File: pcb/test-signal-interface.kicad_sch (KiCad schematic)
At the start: 7 parts, among them J2 BSE-040-01-F-D-A-TR, J3 BSE-040-01-F-D-A-TR, U1 AT24C64D-SSHM-T

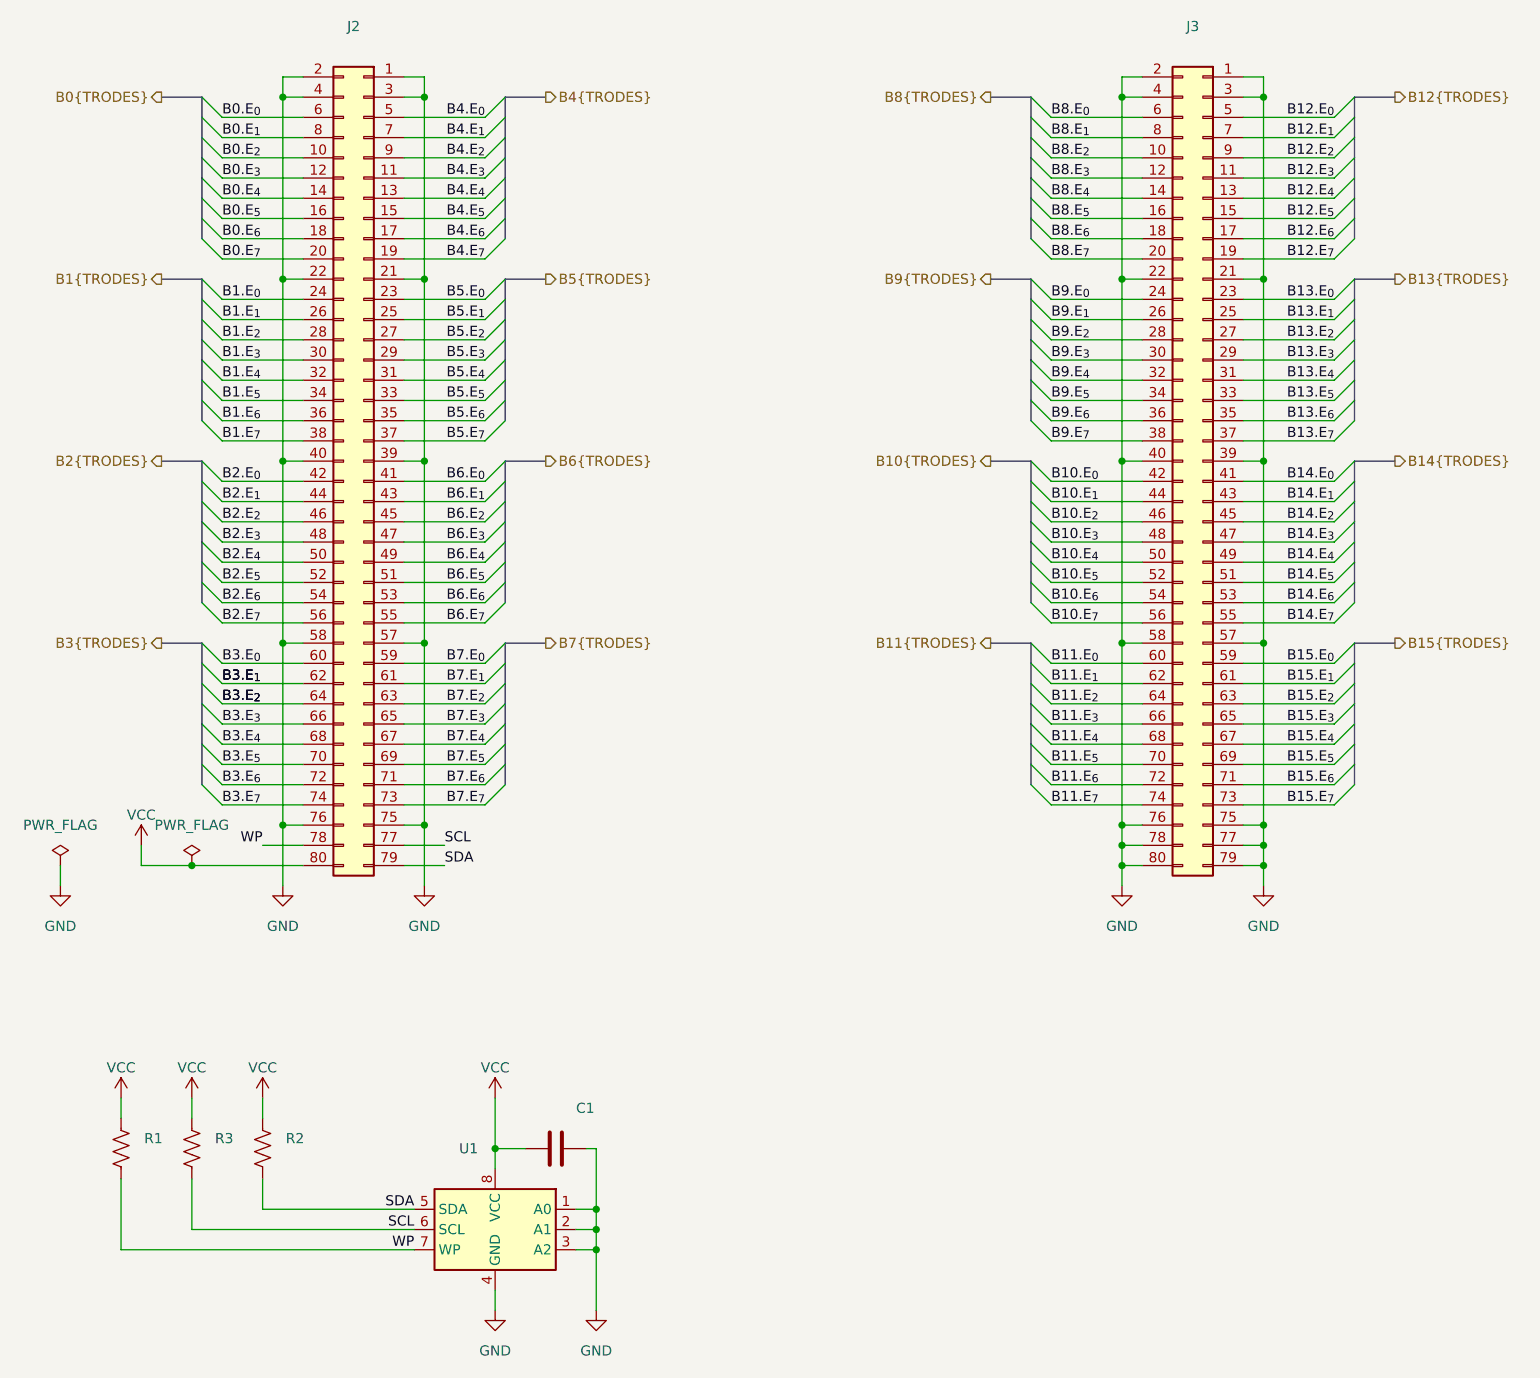
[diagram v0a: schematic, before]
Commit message: details & manufacturing files
- chaged via size D=0.5mm & H=0.2mm
- generated production files
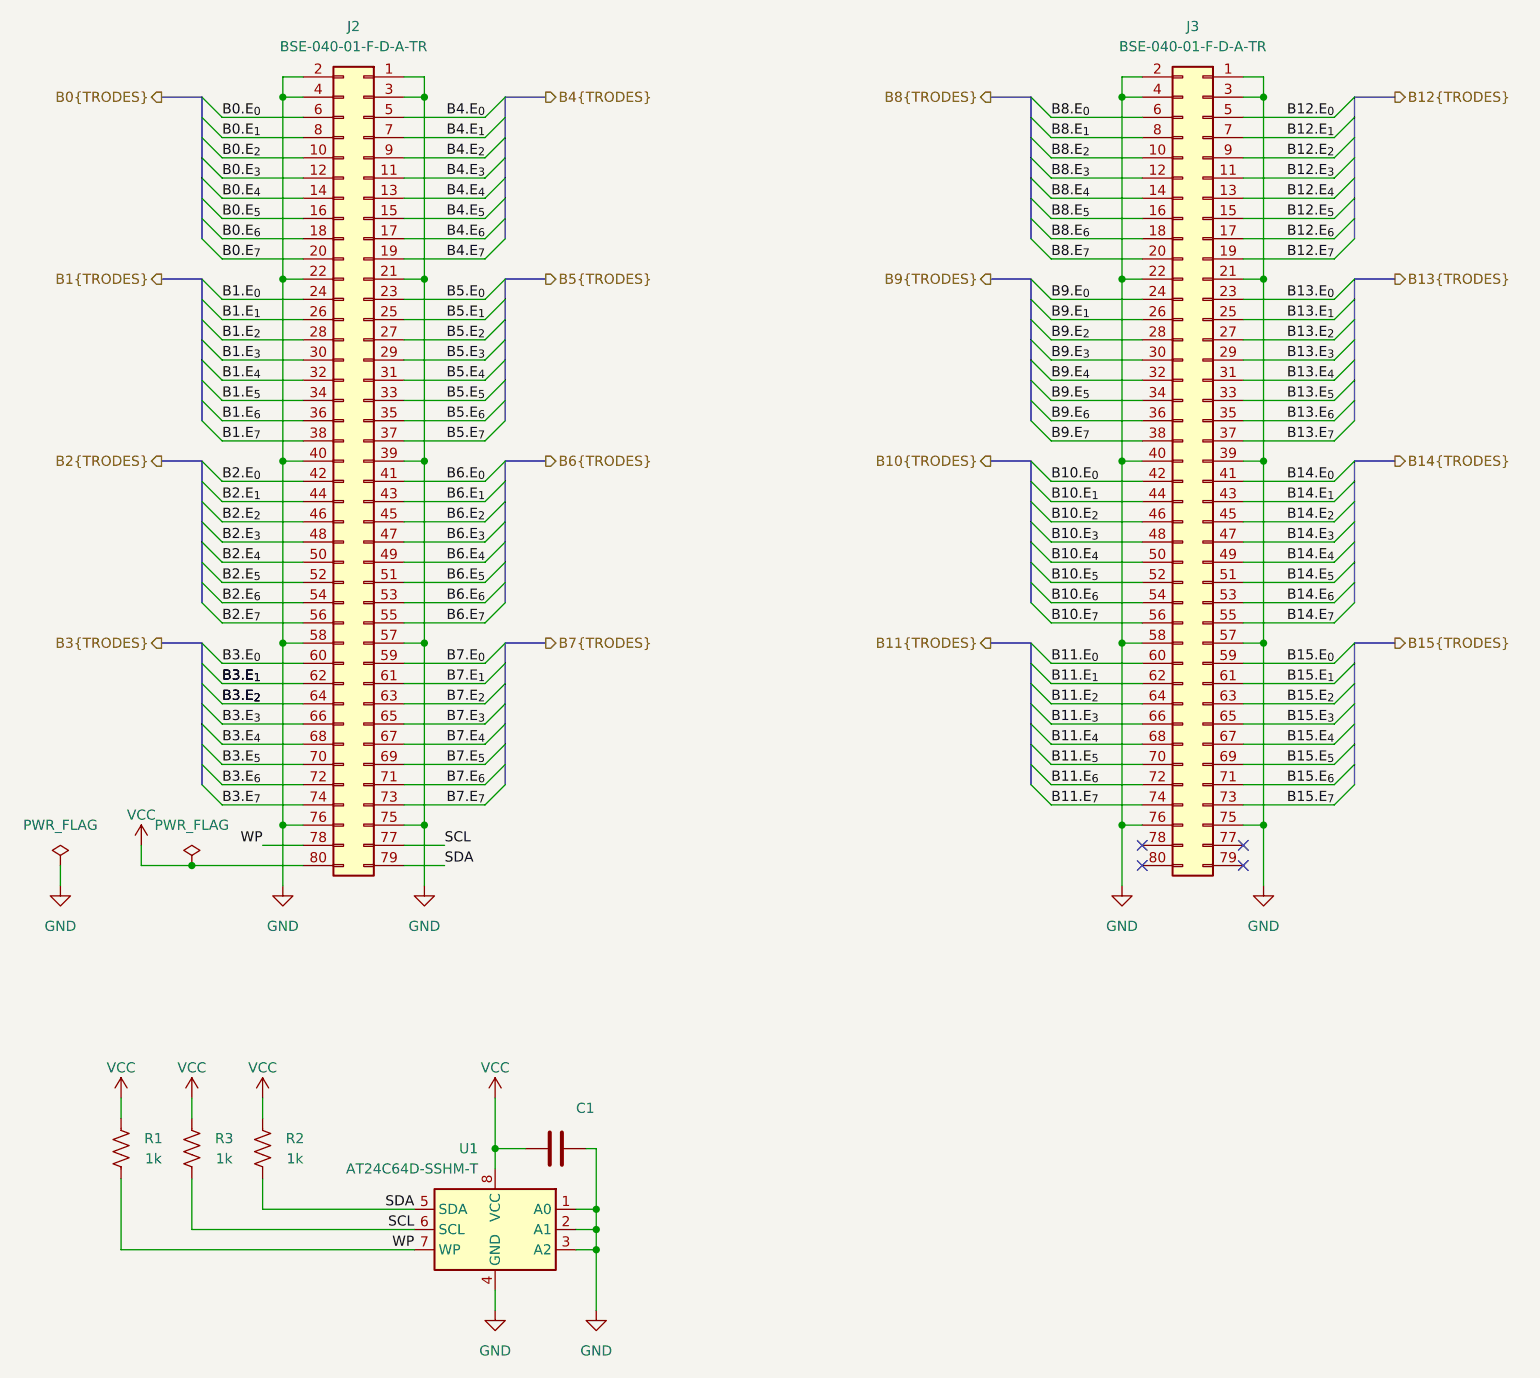
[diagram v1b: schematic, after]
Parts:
- J2, J3: MPN BSE-040-01-X-D-A -> BSE-040-01-F-D-A-TR
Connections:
- net GND: no longer J3.77 (Pin_77), J3.78 (Pin_78), J3.79 (Pin_79), J3.80 (Pin_80)
- no-connect marks 0 -> 4
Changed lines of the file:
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@@
 	)
 	(junction
-		(at 186.69 124.46)
-		(diameter 0)
-		(color 0 0 0 0)
-	)
-	(junction
-		(at 204.47 127)
-		(diameter 0)
-		(color 0 0 0 0)
-	)
-	(junction
 		(at 99.06 53.34)
 		(diameter 0)
@@
 	)
 	(junction
-		(at 186.69 127)
-		(diameter 0)
-		(color 0 0 0 0)
-	)
-	(junction
 		(at 204.47 76.2)
 		(diameter 0)
@@
 	)
 	(junction
-		(at 204.47 124.46)
-		(diameter 0)
-		(color 0 0 0 0)
-	)
-	(junction
 		(at 204.47 53.34)
 		(diameter 0)
@@
 		(color 0 0 0 0)
 	)
+	(no_connect
+		(at 189.23 127)
+	)
+	(no_connect
+		(at 189.23 124.46)
+	)
+	(no_connect
+		(at 201.93 127)
+	)
+	(no_connect
+		(at 201.93 124.46)
+	)
 	(bus_entry
 		(at 71.12 101.6)
@@
 	(wire
 		(pts
-			(xy 186.69 121.92) (xy 186.69 124.46)
+			(xy 186.69 121.92) (xy 186.69 129.54)
 		)
 		(stroke
@@
 	(wire
 		(pts
-			(xy 189.23 124.46) (xy 186.69 124.46)
-		)
-		(stroke
-			(width 0)
-			(type default)
-		)
-	)
-	(wire
-		(pts
 			(xy 73.66 63.5) (xy 83.82 63.5)
 		)
@@
 		)
 	)
-	(wire
-		(pts
-			(xy 204.47 121.92) (xy 204.47 124.46)
-		)
-		(stroke
-			(width 0)
-			(type default)
-		)
-	)
 	(bus
 		(pts
@@
 		)
 	)
-	(wire
-		(pts
-			(xy 186.69 129.54) (xy 186.69 127)
-		)
-		(stroke
-			(width 0)
-			(type default)
-		)
-	)
 	(bus
 		(pts
@@
 	(wire
 		(pts
-			(xy 204.47 127) (xy 204.47 129.54)
+			(xy 204.47 121.92) (xy 204.47 129.54)
 		)
 		(stroke
@@
 		)
 	)
-	(wire
-		(pts
-			(xy 201.93 124.46) (xy 204.47 124.46)
-		)
-		(stroke
-			(width 0)
-			(type default)
-		)
-	)
 	(bus
 		(pts
@@
 	(wire
 		(pts
-			(xy 204.47 124.46) (xy 204.47 127)
-		)
-		(stroke
-			(width 0)
-			(type default)
-		)
-	)
-	(wire
-		(pts
 			(xy 96.52 33.02) (xy 106.68 33.02)
 		)
@@
 	(wire
 		(pts
-			(xy 201.93 127) (xy 204.47 127)
-		)
-		(stroke
-			(width 0)
-			(type default)
-		)
-	)
-	(wire
-		(pts
 			(xy 201.93 83.82) (xy 213.36 83.82)
 		)
@@
 	(wire
 		(pts
-			(xy 186.69 127) (xy 189.23 127)
-		)
-		(stroke
-			(width 0)
-			(type default)
-		)
-	)
-	(wire
-		(pts
 			(xy 186.69 99.06) (xy 186.69 121.92)
 		)
@@
 	(wire
 		(pts
-			(xy 186.69 124.46) (xy 186.69 127)
-		)
-		(stroke
-			(width 0)
-			(type default)
-		)
-	)
-	(wire
-		(pts
 			(xy 177.8 116.84) (xy 189.23 116.84)
 		)
@@
 					(size 1.27 1.27)
 				)
-				(hide yes)
 			)
 		)
@@
 			)
 		)
-		(property "MPN" "BSE-040-01-X-D-A"
+		(property "MPN" "BSE-040-01-F-D-A-TR"
 			(at 91.44 76.2 0)
 			(effects
@@
 					(size 1.27 1.27)
 				)
-				(hide yes)
 			)
 		)
@@
 			)
 		)
-		(property "MPN" "BSE-040-01-X-D-A"
+		(property "MPN" "BSE-040-01-F-D-A-TR"
 			(at 196.85 76.2 0)
 			(effects
@@
 					(size 1.27 1.27)
 				)
-				(hide yes)
 			)
 		)
@@
 					(size 1.27 1.27)
 				)
-				(hide yes)
 			)
 		)
@@
 					(size 1.27 1.27)
 				)
-				(hide yes)
 			)
 		)
@@
 				)
 				(justify left)
-				(hide yes)
 			)
 		)

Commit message: Libraries links updated
Removed local Libraries from Project
. KiCAD libraries
. open-ephys kicad library
. jonnew library

Created new manufacturing files
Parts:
- J2, J3: footprint _footprint Lib:SAMTEC_BSE-040-01-X-D-A -> jonnew:SAMTEC_BSE-040-01-X-D-A; symbol _symbol Lib:Conn_02x40_Odd_Even -> Connector_Generic:Conn_02x40_Odd_Even
- U1: symbol _symbol Lib:AT24CS01-SSHM -> Memory_EEPROM:AT24CS01-SSHM
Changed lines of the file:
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@@
 	)
 	(symbol
-		(lib_id "_symbol Lib:Conn_02x40_Odd_Even")
+		(lib_id "Connector_Generic:Conn_02x40_Odd_Even")
 		(at 91.44 76.2 0)
 		(mirror y)
@@
 			)
 		)
-		(property "Footprint" "_footprint Lib:SAMTEC_BSE-040-01-X-D-A"
+		(property "Footprint" "jonnew:SAMTEC_BSE-040-01-X-D-A"
 			(at 91.44 76.2 0)
 			(effects
@@
 	)
 	(symbol
-		(lib_id "_symbol Lib:Conn_02x40_Odd_Even")
+		(lib_id "Connector_Generic:Conn_02x40_Odd_Even")
 		(at 196.85 76.2 0)
 		(mirror y)
@@
 			)
 		)
-		(property "Footprint" "_footprint Lib:SAMTEC_BSE-040-01-X-D-A"
+		(property "Footprint" "jonnew:SAMTEC_BSE-040-01-X-D-A"
 			(at 196.85 76.2 0)
 			(effects
@@
 	)
 	(symbol
-		(lib_id "_symbol Lib:AT24CS01-SSHM")
+		(lib_id "Memory_EEPROM:AT24CS01-SSHM")
 		(at 107.95 172.72 0)
 		(mirror y)
